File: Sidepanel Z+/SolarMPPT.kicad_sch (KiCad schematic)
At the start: 38 parts

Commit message: Next fix
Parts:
- SC1, SC2: value (none) -> Solar_Cell; footprint (none) -> STS_Solarcells:3G30A_40x80
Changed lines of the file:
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@@
       (effects (font (size 1.27 1.27)) (justify left))
     )
-    (property "Value" "" (id 1) (at 43.18 119.7609 0)
-      (effects (font (size 1.27 1.27)) (justify left))
-    )
-    (property "Footprint" "" (id 2) (at 39.37 119.126 90)
+    (property "Value" "Solar_Cell" (id 1) (at 43.18 119.7609 0)
+      (effects (font (size 1.27 1.27)) (justify left))
+    )
+    (property "Footprint" "STS_Solarcells:3G30A_40x80" (id 2) (at 39.37 119.126 90)
       (effects (font (size 1.27 1.27)) hide)
     )
@@
       (effects (font (size 1.27 1.27)) (justify left))
     )
-    (property "Value" "" (id 1) (at 43.18 52.4509 0)
-      (effects (font (size 1.27 1.27)) (justify left))
-    )
-    (property "Footprint" "" (id 2) (at 39.37 51.816 90)
-      (effects (font (size 1.27 1.27)) hide)
-    )
+    (property "Value" "Solar_Cell" (id 1) (at 43.18 52.4509 0)
+      (effects (font (size 1.27 1.27)) (justify left))
+    )
+    (property "Footprint" "STS_Solarcells:3G30A_40x80" (id 2) (at 39.37 51.816 90)
+      (effects (font (size 1.27 1.27)) hide)
+    )

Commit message: release_2.0, Ordered PCBs
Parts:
- DOUT1: footprint Diode_SMD:D_0603_1608Metric -> SamacSys:STMITE
- DOUT2: footprint LED_SMD:LED_0603_1608Metric -> SamacSys:STMITE
- L_IN1, L_IN2: value 10u -> (none); footprint Inductor_SMD:L_0805_2012Metric -> (none)
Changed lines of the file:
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@@
     (in_bom yes) (on_board yes)
     (property "Reference" "L_IN2" (id 0) (at 100.33 109.22 90))
-    (property "Value" "10u" (id 1) (at 100.33 111.76 90))
-    (property "Footprint" "Inductor_SMD:L_0805_2012Metric" (id 2) (at 100.33 114.3 0)
+    (property "Value" "" (id 1) (at 100.33 111.76 90))
+    (property "Footprint" "" (id 2) (at 100.33 114.3 0)
       (effects (font (size 1.27 1.27)) hide)
     )
@@
       (effects (font (size 1.27 1.27)) (justify left))
     )
-    (property "Footprint" "LED_SMD:LED_0603_1608Metric" (id 2) (at 161.29 97.79 0)
+    (property "Footprint" "SamacSys:STMITE" (id 2) (at 161.29 97.79 0)
       (effects (font (size 1.27 1.27)) hide)
     )
@@
     (in_bom yes) (on_board yes) (fields_autoplaced)
     (property "Reference" "L_IN1" (id 0) (at 100.33 41.91 90))
-    (property "Value" "10u" (id 1) (at 100.33 44.45 90))
-    (property "Footprint" "Inductor_SMD:L_0805_2012Metric" (id 2) (at 100.33 46.99 0)
+    (property "Value" "" (id 1) (at 100.33 44.45 90))
+    (property "Footprint" "" (id 2) (at 100.33 46.99 0)
       (effects (font (size 1.27 1.27)) hide)
     )
@@
       (effects (font (size 1.27 1.27)) (justify left))
     )
-    (property "Footprint" "Diode_SMD:D_0603_1608Metric" (id 2) (at 161.29 30.48 0)
-      (effects (font (size 1.27 1.27)) hide)
-    )
+    (property "Footprint" "SamacSys:STMITE" (id 2) (at 161.29 30.48 0)
+      (effects (font (size 1.27 1.27)) hide)
+    )

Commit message: changed the outline of the pcbs + new axis orientaion + changed the footprint of the solar cells
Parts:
- added D1, D2: PMEG2020EH, Diode_SMD:D_SOD-123F, symbol Diode:PMEG2020EH
- L_IN1, L_IN2: value (none) -> 10u; footprint (none) -> STS_Inductor_SMD:XAL6060103MEC
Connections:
- net MPPT1_IN: now also D1.2 (A)
- net MPPT1_OUT: now also D1.1 (K)
- net MPPT2_IN: now also D2.2 (A)
- net MPPT2_OUT: now also D2.1 (K)

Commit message: small adjustments
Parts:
- R21, R22: value tbd -> 330k
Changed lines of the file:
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@@
       (effects (font (size 1.27 1.27)) (justify right))
     )
-    (property "Value" "tbd" (id 1) (at 179.07 62.2299 0)
+    (property "Value" "330k" (id 1) (at 179.07 62.2299 0)
       (effects (font (size 1.27 1.27)) (justify right))
     )
@@
       (effects (font (size 1.27 1.27)) (justify right))
     )
-    (property "Value" "tbd" (id 1) (at 179.07 129.5399 0)
-      (effects (font (size 1.27 1.27)) (justify right))
-    )
+    (property "Value" "330k" (id 1) (at 179.07 129.5399 0)
+      (effects (font (size 1.27 1.27)) (justify right))
+    )

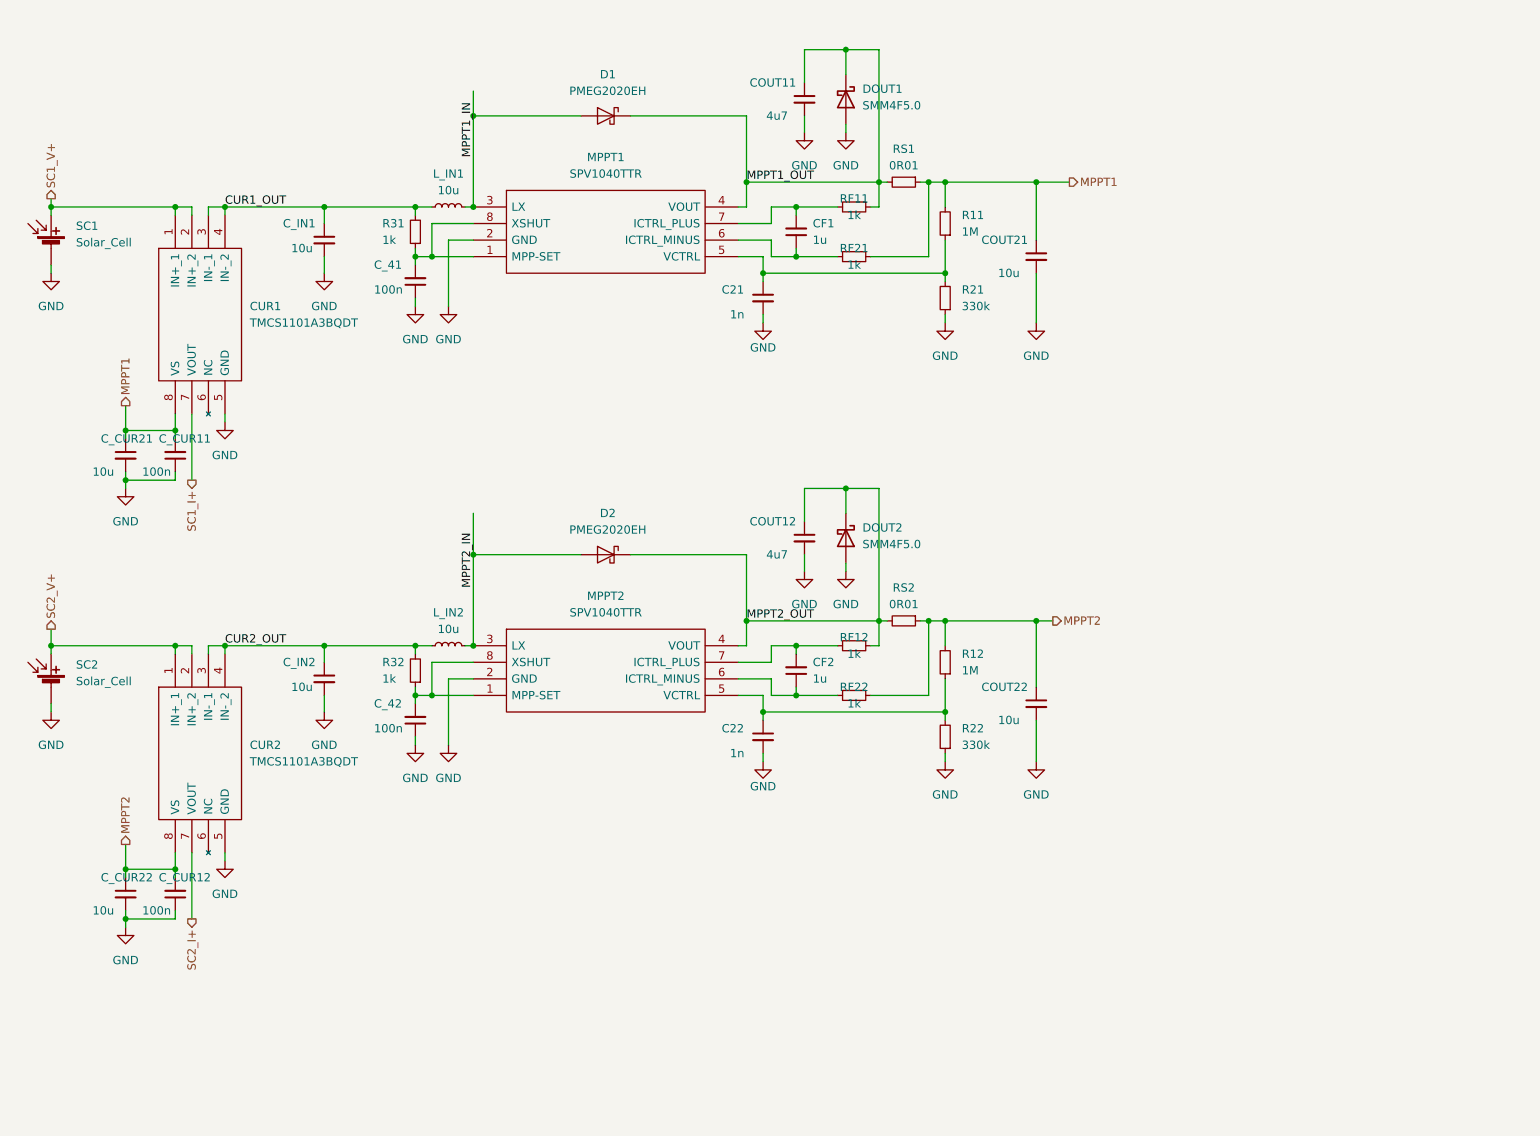
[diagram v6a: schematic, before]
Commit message: changes to the solar cell footprint + added alternative current sensing solution
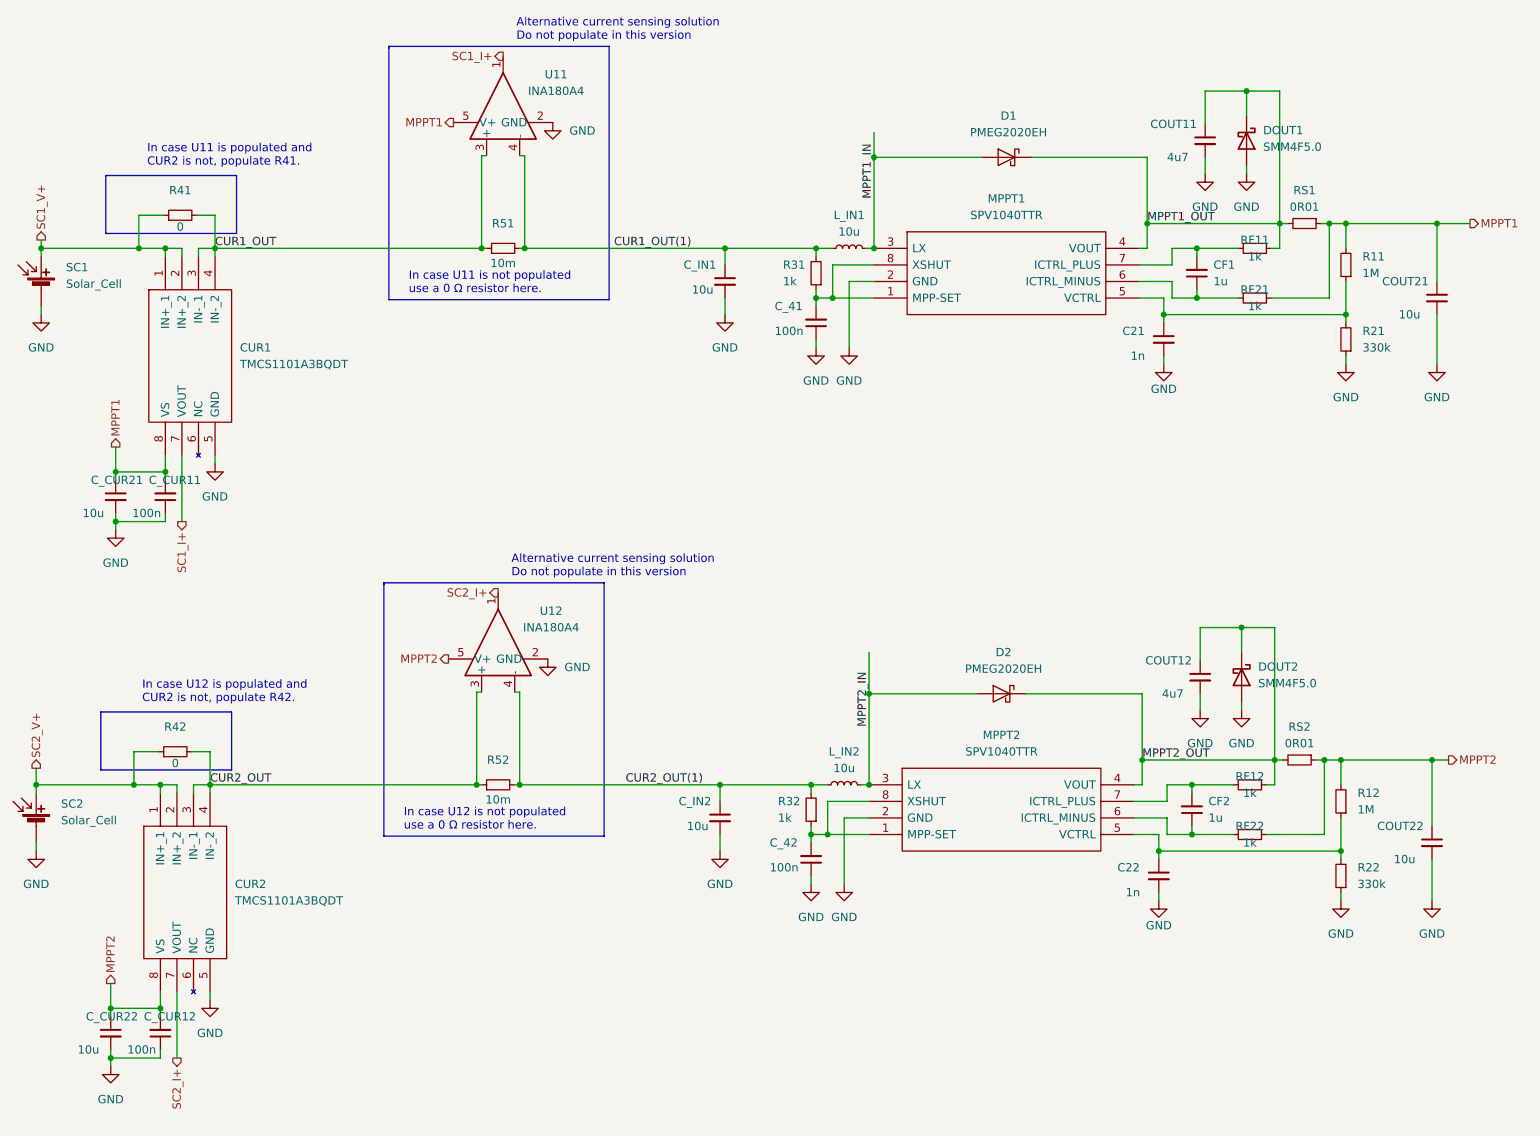
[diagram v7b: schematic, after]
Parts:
- added R41, R42: 0, Resistor_SMD:R_0603_1608Metric, symbol Device:R_Small
- added R51, R52: 10m, Resistor_SMD:R_0603_1608Metric, symbol Device:R_Small
- added U11, U12: INA180A4, Package_TO_SOT_SMD:SOT-23-5, symbol Amplifier_Current:INA180A4
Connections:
- net CUR1_OUT: now also R41.2, R51.1, U11.3 (+); no longer C_IN1.1, L_IN1.1, R31.2
- net CUR2_OUT: now also R42.2, R52.1, U12.3 (+); no longer C_IN2.1, L_IN2.1, R32.2
- net GND: now also U11.2 (GND), U12.2 (GND)
- net MPPT1: now also U11.5 (V+)
- net MPPT2: now also U12.5 (V+)
- net SC1_I+: now also U11.1
- net SC1_V+: now also R41.1
- net SC2_I+: now also U12.1
- net SC2_V+: now also R42.1
- new net CUR1_OUT(1): C_IN1.1, L_IN1.1, R31.2, R51.2, U11.4 (-)
- new net CUR2_OUT(1): C_IN2.1, L_IN2.1, R32.2, R52.2, U12.4 (-)
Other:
- note added: "Alternative current sensing solution Do not populate in this version"
- note added: "In case U11 is not populated use a 0 Ω resistor here."
- note added: "In case U11 is populated and CUR2 is not, populate R41."
- note added: "In case U12 is not populated use a 0 Ω resistor here."
- note added: "In case U12 is populated and CUR2 is not, populate R42."
- moved on the sheet: C21, C22, CF1, CF2, COUT11, COUT12, COUT21, COUT22, CUR1, CUR2, C_41, C_42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

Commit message: added the libraries for the specific components
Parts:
- SC1: footprint STS_Solarcells:3G30A_40x80 -> STS_solder:3G30A_40x80_Z_SC1
- SC2: footprint STS_Solarcells:3G30A_40x80 -> STS_solder:3G30A_40x80_Z_SC2
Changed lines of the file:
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@@
       (effects (font (size 1.27 1.27)) (justify left))
     )
-    (property "Footprint" "STS_Solarcells:3G30A_40x80" (id 2) (at 37.084 140.462 90)
+    (property "Footprint" "STS_solder:3G30A_40x80_Z_SC2" (id 2) (at 37.084 140.462 90)
       (effects (font (size 1.27 1.27)) hide)
     )
@@
       (effects (font (size 1.27 1.27)) (justify left))
     )
-    (property "Footprint" "STS_Solarcells:3G30A_40x80" (id 2) (at 37.846 58.166 90)
-      (effects (font (size 1.27 1.27)) hide)
-    )
+    (property "Footprint" "STS_solder:3G30A_40x80_Z_SC1" (id 2) (at 37.846 58.166 90)
+      (effects (font (size 1.27 1.27)) hide)
+    )
